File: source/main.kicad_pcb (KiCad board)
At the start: 2 copper layers, 0 parts

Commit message: Proof of life
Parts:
- added R1: 1kΩ ±1% 62.5mW, lcsc:R0402, F.Cu at (120.7, 81.5)

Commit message: Add ESP32 module
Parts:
- added C1: 20pF ±5% 50V C0G, lcsc:C0402, F.Cu at (74.7, 91.1)
- added R1: 1kΩ ±1% 62.5mW, lcsc:R0402, F.Cu at (90.0, 77.1)
- added R2: 100Ω, lcsc:R0402, F.Cu at (90.0, 79.3)
- added R3: 100Ω, lcsc:R0402, F.Cu at (90.0, 81.4)
- added R4: 100Ω, lcsc:R0402, F.Cu at (90.0, 83.6)
- added U1: ESP32_C3_MINI_1, lcsc:WIFIM-SMD_ESP32-C3-MINI-MINI-1U, F.Cu at (81.2, 83.7)
- moved R1 20.6 mm to (101.3, 74.4)

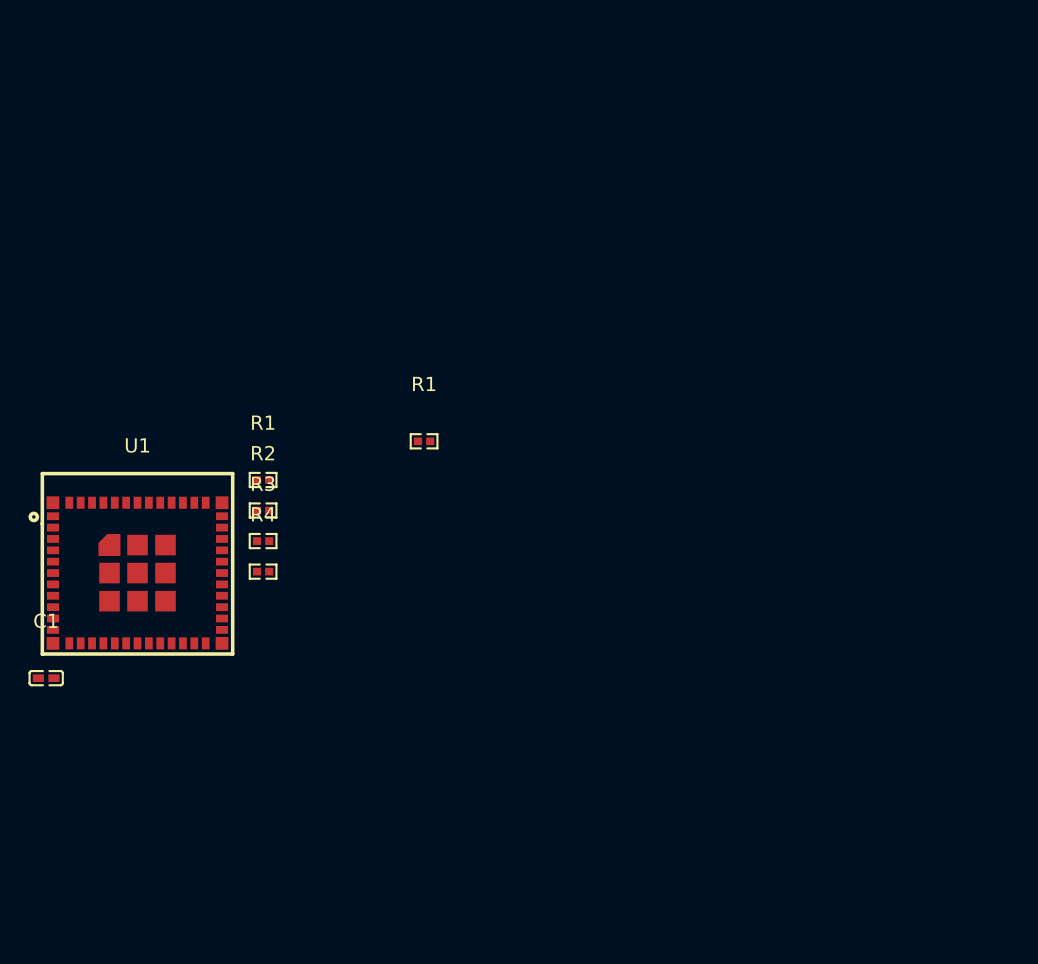
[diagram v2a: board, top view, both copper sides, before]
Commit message: KiCAD resources reloaded
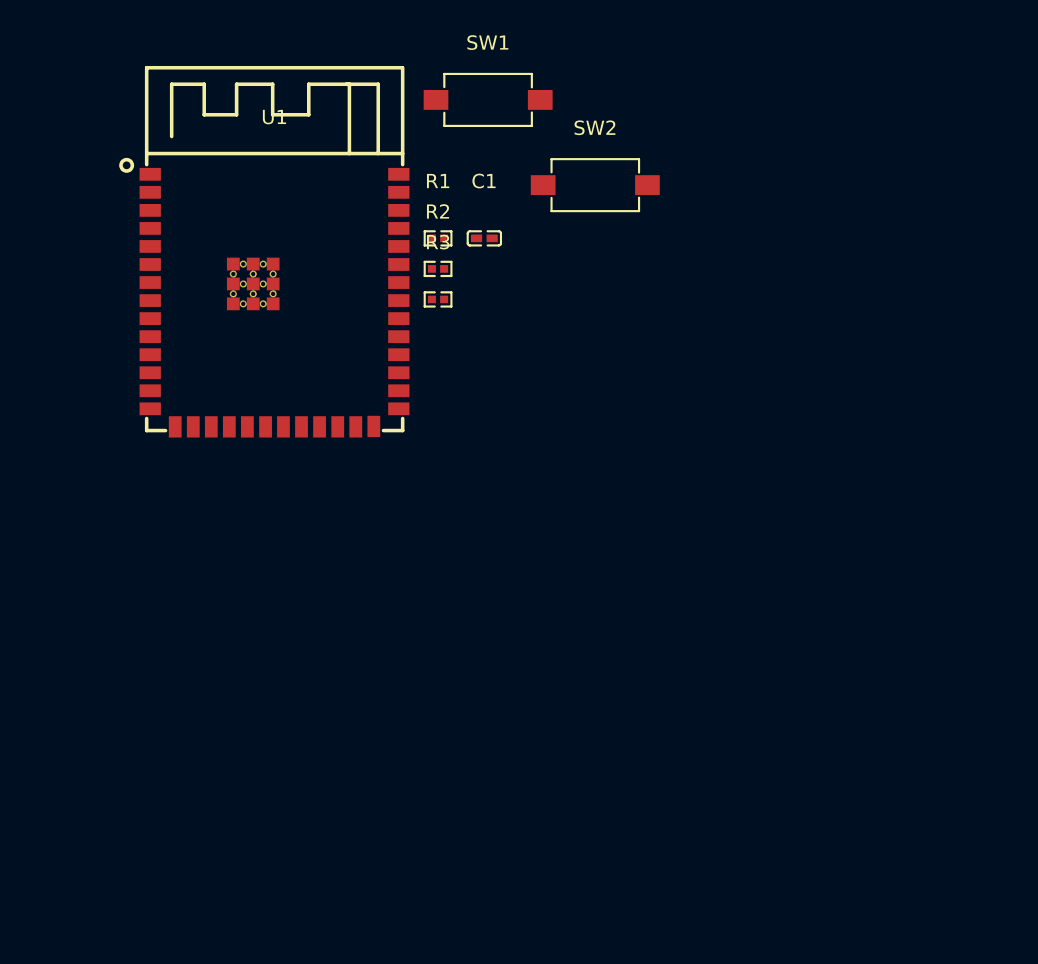
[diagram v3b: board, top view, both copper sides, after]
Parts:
- removed the R1 at (101.3, 74.4)
- removed the R1 at (90.0, 77.1)
- removed R4: 100Ω, lcsc:R0402
- added R1: 10kΩ ±1% 62.5mW, lcsc:R0402, F.Cu at (102.3, 60.1)
- added SW1: Switch2, lcsc:SW-SMD_L6.0-W3.5-LS8.0, F.Cu at (105.9, 50.4)
- added SW2: Switch2, lcsc:SW-SMD_L6.0-W3.5-LS8.0, F.Cu at (113.4, 56.4)
- R2: value 100Ω -> 10kΩ ±1% 62.5mW
- R3: value 100Ω -> 1kΩ ±1% 62.5mW
- U1: value ESP32_C3_MINI_1 -> ESP32_S3_WROOM_1_N16R8; footprint lcsc:WIFIM-SMD_ESP32-C3-MINI-MINI-1U -> lcsc:WIRELM-SMD_ESP32-S3-WROOM-1
- moved C1 43.7 mm to (105.6, 60.1)
- moved U1 21.5 mm to (90.8, 64.5)
- moved R2 21.0 mm to (102.3, 62.3)
- moved R3 21.0 mm to (102.3, 64.4)
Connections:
- C1 pad 1: C1-1-U1-3 -> C1-1-U1-2
- C1 pad 2: C1-2-U1-1-U1-11-U1-14-U1-2-U1-36-U1-37-U1-38-U1-39-U1-40-U1-41-U1-42-U1-43-U1-44-U1-45-U1-46-U1-47-U1-48-U1-49-U1-50-U1-51-U1-52-U1-53 -> C1-2-SW1-2-SW2-2-U1-1-U1-40-U1-41
- R2 pad 1: R2-1-U1-8 -> R2-1-SW2-1
- R3 pad 1: R3-1-U1-5 -> R3-1
- U1 pad 1: C1-2-U1-1-U1-11-U1-14-U1-2-U1-36-U1-37-U1-38-U1-39-U1-40-U1-41-U1-42-U1-43-U1-44-U1-45-U1-46-U1-47-U1-48-U1-49-U1-50-U1-51-U1-52-U1-53 -> C1-2-SW1-2-SW2-2-U1-1-U1-40-U1-41
- U1 pad 11: C1-2-U1-1-U1-11-U1-14-U1-2-U1-36-U1-37-U1-38-U1-39-U1-40-U1-41-U1-42-U1-43-U1-44-U1-45-U1-46-U1-47-U1-48-U1-49-U1-50-U1-51-U1-52-U1-53 -> U1-11
- U1 pad 14: C1-2-U1-1-U1-11-U1-14-U1-2-U1-36-U1-37-U1-38-U1-39-U1-40-U1-41-U1-42-U1-43-U1-44-U1-45-U1-46-U1-47-U1-48-U1-49-U1-50-U1-51-U1-52-U1-53 -> U1-14
- U1 pad 2: C1-2-U1-1-U1-11-U1-14-U1-2-U1-36-U1-37-U1-38-U1-39-U1-40-U1-41-U1-42-U1-43-U1-44-U1-45-U1-46-U1-47-U1-48-U1-49-U1-50-U1-51-U1-52-U1-53 -> C1-1-U1-2
- U1 pad 22: R4-1-U1-22 -> U1-22
- U1 pad 3: C1-1-U1-3 -> U1-3
- U1 pad 36: C1-2-U1-1-U1-11-U1-14-U1-2-U1-36-U1-37-U1-38-U1-39-U1-40-U1-41-U1-42-U1-43-U1-44-U1-45-U1-46-U1-47-U1-48-U1-49-U1-50-U1-51-U1-52-U1-53 -> U1-36
- U1 pad 37: C1-2-U1-1-U1-11-U1-14-U1-2-U1-36-U1-37-U1-38-U1-39-U1-40-U1-41-U1-42-U1-43-U1-44-U1-45-U1-46-U1-47-U1-48-U1-49-U1-50-U1-51-U1-52-U1-53 -> U1-37
- U1 pad 38: C1-2-U1-1-U1-11-U1-14-U1-2-U1-36-U1-37-U1-38-U1-39-U1-40-U1-41-U1-42-U1-43-U1-44-U1-45-U1-46-U1-47-U1-48-U1-49-U1-50-U1-51-U1-52-U1-53 -> U1-38
- U1 pad 39: C1-2-U1-1-U1-11-U1-14-U1-2-U1-36-U1-37-U1-38-U1-39-U1-40-U1-41-U1-42-U1-43-U1-44-U1-45-U1-46-U1-47-U1-48-U1-49-U1-50-U1-51-U1-52-U1-53 -> U1-39
- U1 pad 40: C1-2-U1-1-U1-11-U1-14-U1-2-U1-36-U1-37-U1-38-U1-39-U1-40-U1-41-U1-42-U1-43-U1-44-U1-45-U1-46-U1-47-U1-48-U1-49-U1-50-U1-51-U1-52-U1-53 -> C1-2-SW1-2-SW2-2-U1-1-U1-40-U1-41
- U1 pad 41: C1-2-U1-1-U1-11-U1-14-U1-2-U1-36-U1-37-U1-38-U1-39-U1-40-U1-41-U1-42-U1-43-U1-44-U1-45-U1-46-U1-47-U1-48-U1-49-U1-50-U1-51-U1-52-U1-53 -> C1-2-SW1-2-SW2-2-U1-1-U1-40-U1-41
- U1 pad 5: R3-1-U1-5 -> U1-5
- U1 pad 8: R2-1-U1-8 -> U1-8

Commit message: Add DRV8300 power-stage
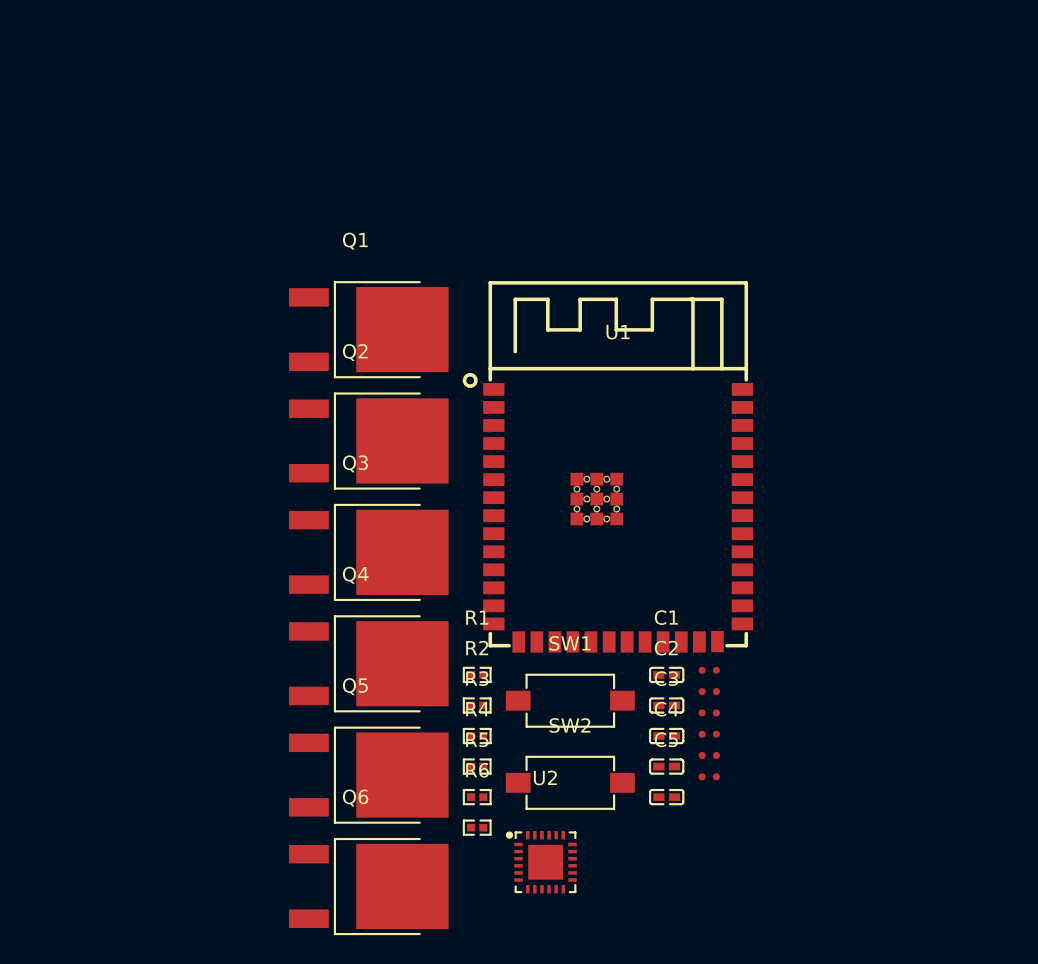
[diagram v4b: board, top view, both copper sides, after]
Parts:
- added C2: 20pF ±5% 50V C0G, lcsc:C0402, F.Cu at (118.4, 93.0)
- added C3: 20pF ±5% 50V C0G, lcsc:C0402, F.Cu at (118.4, 95.2)
- added C4: 20pF ±5% 50V C0G, lcsc:C0402, F.Cu at (118.4, 97.3)
- added C5: 220pF ±10% 50V X7R, lcsc:C0402, F.Cu at (118.4, 99.5)
- added H1: NetTie, NetTie:NetTie-2_SMD_Pad0.5mm, F.Cu at (121.4, 90.5)
- added H2: NetTie, NetTie:NetTie-2_SMD_Pad0.5mm, F.Cu at (121.4, 92.0)
- added H3: NetTie, NetTie:NetTie-2_SMD_Pad0.5mm, F.Cu at (121.4, 93.5)
- added H4: NetTie, NetTie:NetTie-2_SMD_Pad0.5mm, F.Cu at (121.4, 95.0)
- added H5: NetTie, NetTie:NetTie-2_SMD_Pad0.5mm, F.Cu at (121.4, 96.5)
- added H6: NetTie, NetTie:NetTie-2_SMD_Pad0.5mm, F.Cu at (121.4, 98.0)
- added Q1: MOSFET, lcsc:TO-252-2_L6.6-W6.1-P4.57-LS9.9-TL-CW, F.Cu at (96.5, 66.6)
- added Q2: MOSFET, lcsc:TO-252-2_L6.6-W6.1-P4.57-LS9.9-TL-CW, F.Cu at (96.5, 74.4)
- added Q3: MOSFET, lcsc:TO-252-2_L6.6-W6.1-P4.57-LS9.9-TL-CW, F.Cu at (96.5, 82.2)
- added Q4: MOSFET, lcsc:TO-252-2_L6.6-W6.1-P4.57-LS9.9-TL-CW, F.Cu at (96.5, 90.1)
- added Q5: MOSFET, lcsc:TO-252-2_L6.6-W6.1-P4.57-LS9.9-TL-CW, F.Cu at (96.5, 97.9)
- added Q6: MOSFET, lcsc:TO-252-2_L6.6-W6.1-P4.57-LS9.9-TL-CW, F.Cu at (96.5, 105.8)
- added R4: 100Ω, lcsc:R0402, F.Cu at (105.1, 97.3)
- added R5: 100Ω, lcsc:R0402, F.Cu at (105.1, 99.5)
- added R6: 100Ω, lcsc:R0402, F.Cu at (105.1, 101.6)
- added U2: DRV8300, lcsc:VQFN-24_L4.0-W4.0-P0.50-TL-EP2.5, F.Cu at (109.9, 104.1)
- SW1, SW2: value Switch2 -> _Switch
- moved SW1 42.7 mm to (111.6, 92.7)
- moved SW2 42.1 mm to (111.6, 98.5)
- moved C1 33.3 mm to (118.4, 90.9)
- moved R2 30.9 mm to (105.1, 93.0)
- moved R1 30.9 mm to (105.1, 90.9)
- moved R3 30.9 mm to (105.1, 95.2)
- moved U1 28.5 mm to (115.0, 79.7)
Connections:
- C1 pad 1: C1-1-U1-2 -> C1-1-R1-2-R2-2-U1-2
- R1 pad 2: R1-2 -> C1-1-R1-2-R2-2-U1-2
- R2 pad 2: R2-2 -> C1-1-R1-2-R2-2-U1-2
- U1 pad 2: C1-1-U1-2 -> C1-1-R1-2-R2-2-U1-2

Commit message: Upgrade ESP32-S3 to new holders
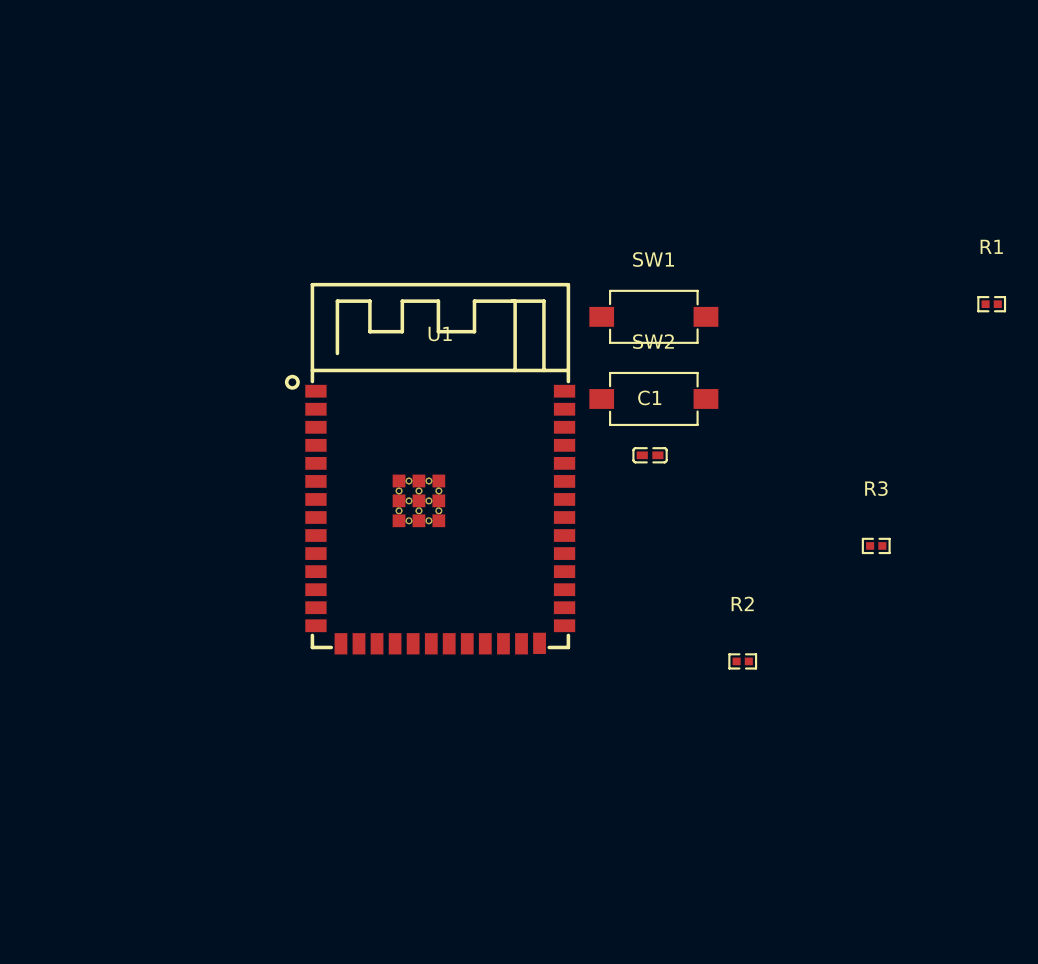
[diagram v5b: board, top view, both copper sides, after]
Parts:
- removed C2, C3, C4: 20pF ±5% 50V C0G, lcsc:C0402
- removed C5: 220pF ±10% 50V X7R, lcsc:C0402
- removed H1, H2, H3, H4, H5, H6: NetTie, NetTie:NetTie-2_SMD_Pad0.5mm
- removed Q1, Q2, Q3, Q4, Q5, Q6: MOSFET, lcsc:TO-252-2_L6.6-W6.1-P4.57-LS9.9-TL-CW
- removed R4, R5, R6: 100Ω, lcsc:R0402
- removed U2: DRV8300, lcsc:VQFN-24_L4.0-W4.0-P0.50-TL-EP2.5
- R1, R2: value 10kΩ ±1% 62.5mW -> 7.5kΩ ±1% 62.5mW
- R3: value 1kΩ ±1% 62.5mW -> 100Ω
- moved R1 44.6 mm to (141.3, 64.8)
- moved R3 31.1 mm to (133.2, 81.8)
- moved SW1 27.7 mm to (117.5, 65.7)
- moved SW2 27.7 mm to (117.5, 71.4)
- moved R2 18.9 mm to (123.8, 89.9)
- moved C1 15.5 mm to (117.3, 75.4)
- moved U1 12.5 mm to (102.5, 79.8)
